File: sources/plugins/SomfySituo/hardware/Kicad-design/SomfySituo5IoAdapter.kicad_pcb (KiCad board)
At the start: 2 copper layers, 25.4 x 21.8 mm, 30 parts, among them J1 USB_OTG, J10 Conn_01x01, J11 Conn_01x01, J12 Conn_01x01, J13 Conn_01x01, J15 ICSP, J2 Conn_01x01, J3 Conn_01x01, J4 Conn_01x01, J5 Conn_01x01, J6 Conn_01x01, J7 Conn_01x01, J8 Conn_01x01, J9 Conn_01x01, U1 FT230X, U2 PIC16F688

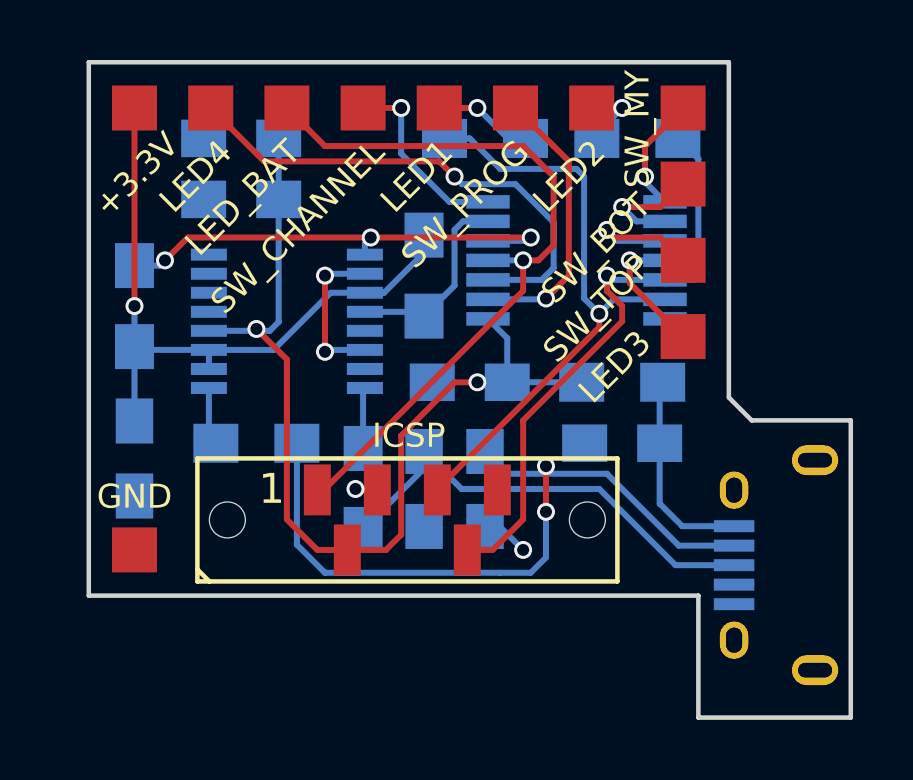
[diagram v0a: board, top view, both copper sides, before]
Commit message: Update USB connector footprint
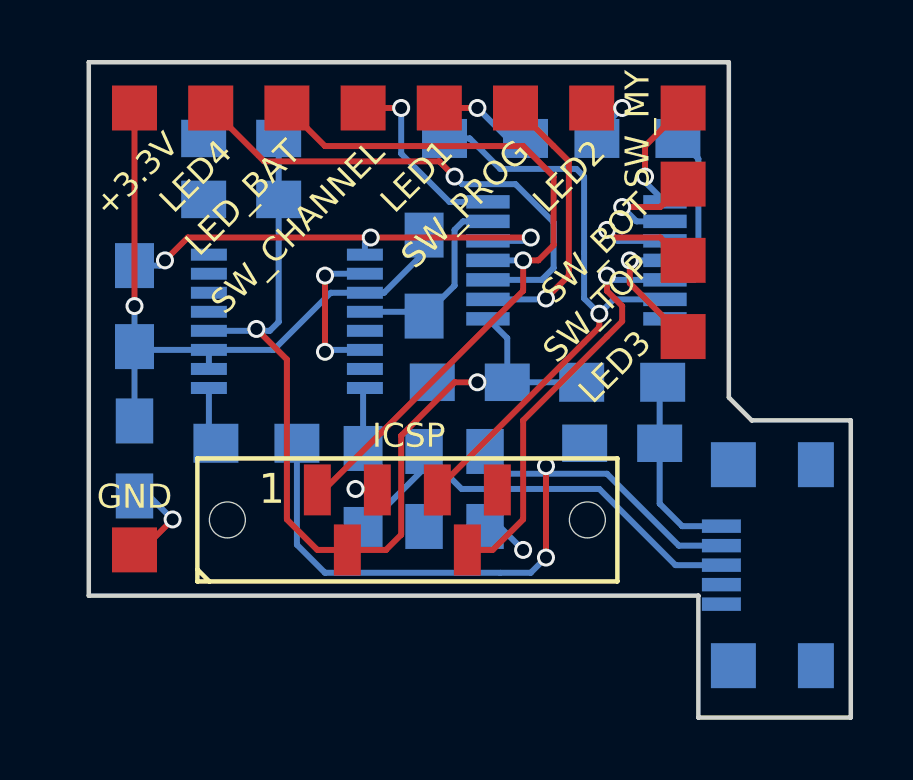
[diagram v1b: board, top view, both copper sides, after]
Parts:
- J1: footprint Connectors:USB_Micro-B -> USB_Micro-B_AC0002646:USB_Micro-B_AC0002646
- moved J1 0.13 mm to (131.2, 127.0)
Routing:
- net GND: track 2.34 -> 5.62 mm, vias 2 -> 3

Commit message: Send PCB to factoring
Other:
- outline, holes or cut-outs redrawn
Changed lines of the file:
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@@
     (links 57)
     (no_connects 0)
-    (area 108.128999 110.160999 133.679001 132.155001)
+    (area 90.194001 97.376 153.138 141.384001)
     (thickness 1.6)
-    (drawings 39)
+    (drawings 41)
     (tracks 194)
     (zones 0)
@@
     (visible_elements 7FFFFF7F)
     (pcbplotparams
-      (layerselection 0x00030_80000001)
+      (layerselection 0x010f0_80000001)
       (usegerberextensions false)
       (excludeedgelayer true)
@@
       (outputformat 1)
       (mirror false)
-      (drillshape 1)
+      (drillshape 0)
       (scaleselection 1)
-      (outputdirectory ""))
+      (outputdirectory out/))
   )
   (net 0 "")
@@
       (net 2 GND))
   )
+  (gr_line (start 128.27 128.016) (end 108.204 128.016) (angle 90) (layer Edge.Cuts) (width 0.15))
+  (gr_line (start 128.524 128.27) (end 128.27 128.016) (angle 90) (layer Edge.Cuts) (width 0.15))
+  (gr_line (start 128.524 132.08) (end 128.524 128.27) (angle 90) (layer Edge.Cuts) (width 0.15))
+  (dimension 25.4 (width 0.3) (layer Cmts.User)
+    (gr_text "25,400 mm" (at 120.904 98.726) (layer Cmts.User)
+      (effects (font (size 1.5 1.5) (thickness 0.3)))
+    )
+    (feature1 (pts (xy 133.604 103.886) (xy 133.604 97.376)))
+    (feature2 (pts (xy 108.204 103.886) (xy 108.204 97.376)))
+    (crossbar (pts (xy 108.204 100.076) (xy 133.604 100.076)))
+    (arrow1a (pts (xy 133.604 100.076) (xy 132.477496 100.662421)))
+    (arrow1b (pts (xy 133.604 100.076) (xy 132.477496 99.489579)))
+    (arrow2a (pts (xy 108.204 100.076) (xy 109.330504 100.662421)))
+    (arrow2b (pts (xy 108.204 100.076) (xy 109.330504 99.489579)))
+  )
   (gr_circle (center 128.27 124.841) (end 128.397 124.841) (layer B.SilkS) (width 0.2))
   (gr_circle (center 117.729 115.697) (end 117.856 115.697) (layer B.SilkS) (width 0.2))
@@
   )
   (gr_line (start 108.204 110.236) (end 129.54 110.236) (angle 90) (layer Edge.Cuts) (width 0.15))
-  (gr_line (start 108.204 128.016) (end 128.524 128.016) (angle 90) (layer Edge.Cuts) (width 0.15))
   (gr_line (start 108.204 110.236) (end 108.204 128.016) (angle 90) (layer Edge.Cuts) (width 0.15))
   (dimension 21.844 (width 0.3) (layer Cmts.User)
@@
     (effects (font (size 1 1) (thickness 0.2)))
   )
-  (gr_line (start 128.524 132.08) (end 128.524 128.016) (angle 90) (layer Edge.Cuts) (width 0.15))
   (gr_line (start 133.604 132.08) (end 128.524 132.08) (angle 90) (layer Edge.Cuts) (width 0.15))
   (segment (start 116.824 126.492) (end 115.824 126.492) (width 0.2) (layer F.Cu) (net 1))
@@
       (pts
         (xy 108.204 110.236) (xy 129.54 110.236) (xy 129.54 121.412) (xy 130.302 122.174) (xy 133.604 122.174)
-        (xy 133.604 132.08) (xy 128.524 132.08) (xy 128.524 128.016) (xy 108.204 128.016)
+        (xy 133.604 132.08) (xy 128.524 132.08) (xy 128.524 128.27) (xy 128.27 128.016) (xy 108.204 128.016)
       )
     )
@@
       (pts
         (xy 108.204 110.236) (xy 129.54 110.236) (xy 129.54 121.412) (xy 130.302 122.174) (xy 133.604 122.174)
-        (xy 133.604 132.08) (xy 128.524 132.08) (xy 128.524 128.016) (xy 108.204 128.016)
+        (xy 133.604 132.08) (xy 128.524 132.08) (xy 128.524 128.27) (xy 128.27 128.016) (xy 108.204 128.016)
       )
     )
